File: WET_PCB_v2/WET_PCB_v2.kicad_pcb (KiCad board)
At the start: 2 copper layers, 100 x 80 mm, 164 parts, among them J1 Capacitor connector, J10 Conn_01x09_Pin, J11 Conn_01x09_Pin, J12 Fuse holder or smth to hold t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, J13 Fuse holder or smth to hold t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, J14 Fuse holder or smth to hold t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, J15 Fuse holder or smth to hold t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, J16 POGO1, J17 Capacitor connector, J18 Capacitor connector, J19 Capacitor connector, J2 Conn_01x09_Pin, J20 Capacitor connector, J21 POGO2, J22 LA55_GND, J23 LA55_M, J24 LA55_+, J25 Capacitor connector, J26 Vsense_ADC1_IN1, J27 Fuse holder or smth to hold t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, J28 Fuse holder or smth to hold t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, J29 Fuse holder or smth to hold t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, J3 Conn_01x09_Pin, J30 Fuse holder or smth to hold t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, J31 Fuse holder or smth to hold t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, J32 Fuse holder or smth to hold t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, J33 Fuse holder or smth to hold t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, J34 Fuse holder or smth to hold t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, J4 Power input, J5 Barrel jack, J6 Coil plug, J7 Pluggable Terminal Block, J8 Jumper, J9 Capacitor connector, Q1 IRF530NPBF, Q2 IRF530NPBF, Q3 IRF530NPBF, Q4 IRF530NPBF, Q5 Q_NMOS_GDS, Q6 Q_NMOS_GDS, U1 IR2110, U2 IR2110, U3 Opamp_Quad, U4 IR2110, U5 LA55-P, U6 L7805

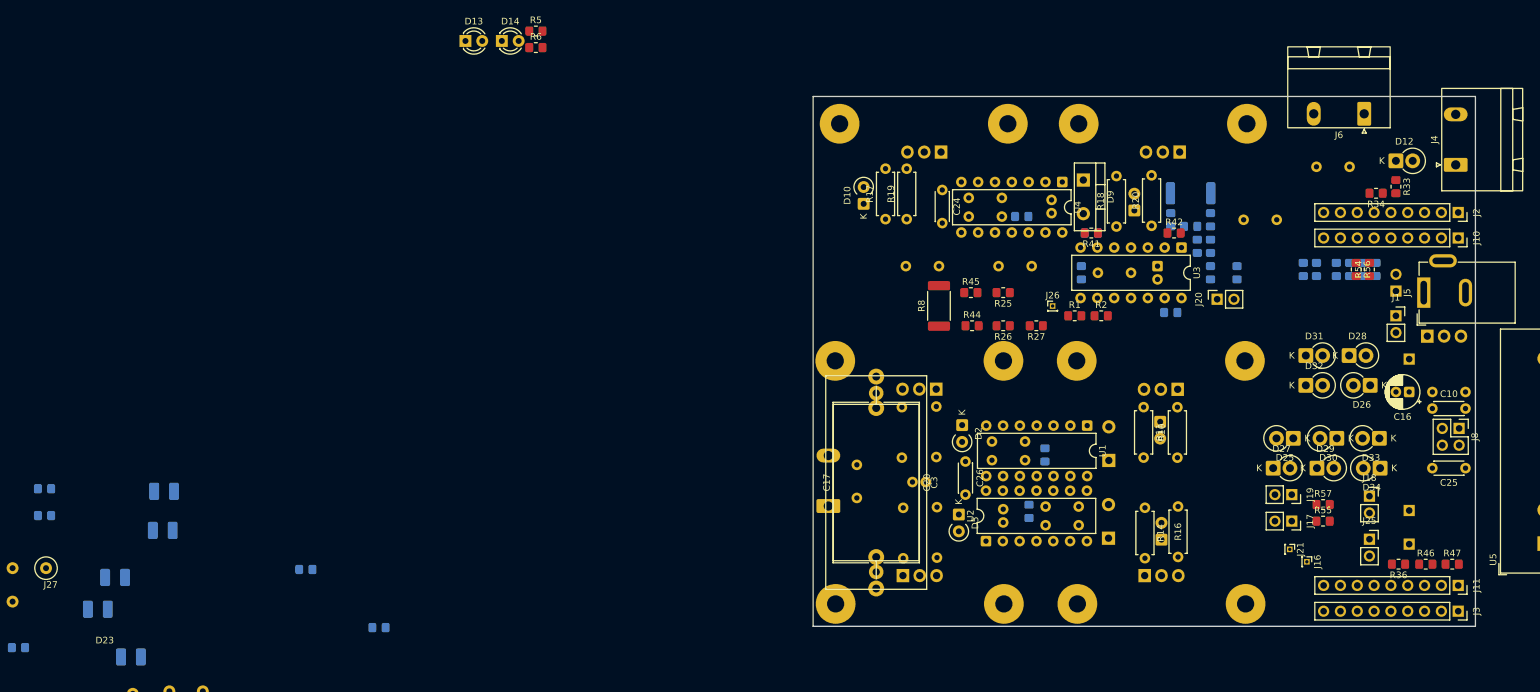
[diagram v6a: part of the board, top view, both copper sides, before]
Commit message: microcontroller to chip traces done
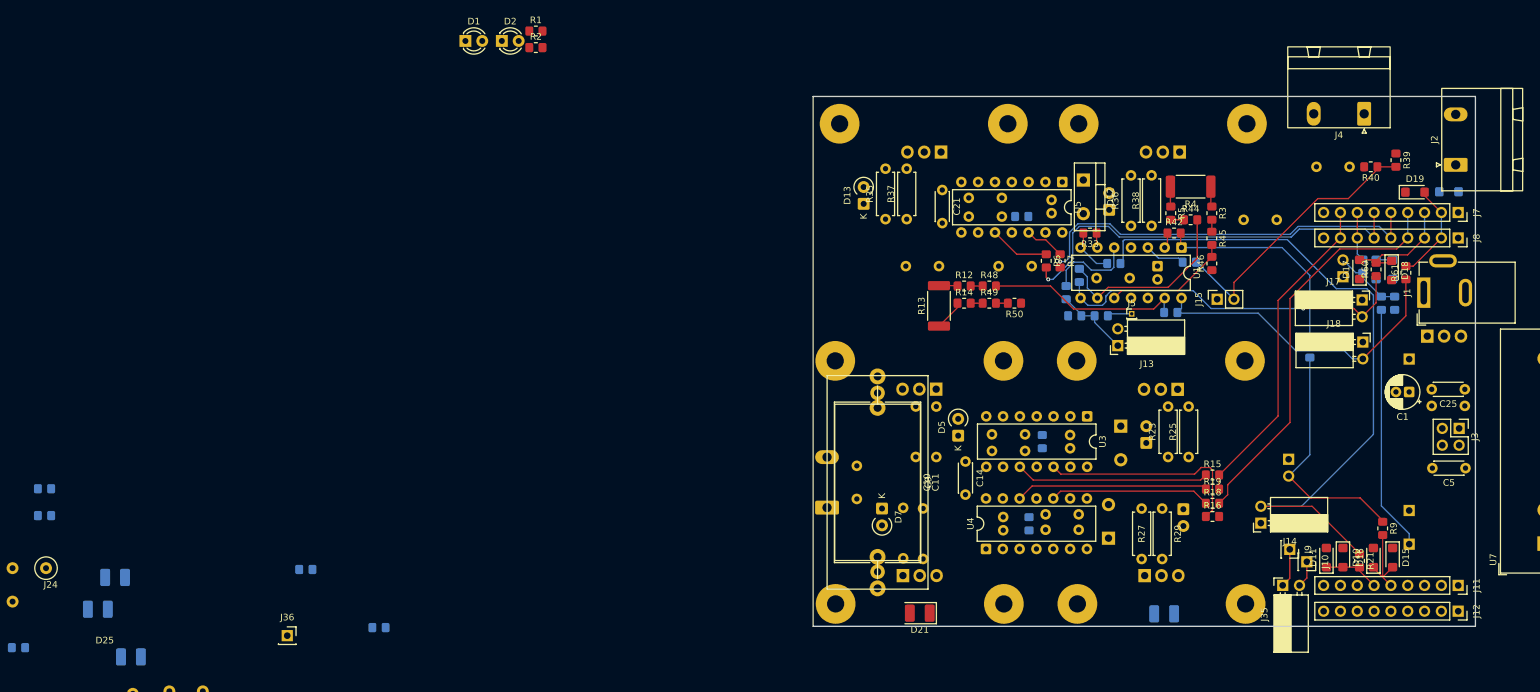
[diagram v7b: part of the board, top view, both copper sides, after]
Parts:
- removed the C17 at (167.5, 154.7)
- removed the C20 at (167.5, 127.4)
- removed the D12 at (246.0, 90.1)
- removed D33, D34: D_Zener, Diode_THT:D_DO-15_P2.54mm_Vertical_CathodeUp
- removed the R54 at (242.0, 106.5)
- removed the R55 at (235.0, 144.5)
- removed the R56 at (240.0, 106.5)
- removed the R57 at (235.0, 142.0)
- added C10: B32529C1104K000, Inductor_THT:L_Axial_L23.4mm_D12.7mm_P32.00mm_Horizontal_Vishay_IHA-203, F.Cu at (167.7, 122.7)
- added C9: B32529C1104K000, Capacitor_THT:C_Rect_L24.0mm_W12.8mm_P22.50mm_MKT, F.Cu at (167.7, 127.4)
- added D27: D_Zener, Diode_SMD:D_SMF, B.Cu at (243.0, 106.5)
- added D28: D_Zener, Diode_SMD:D_SMF, B.Cu at (245.5, 106.5)
- added J35: Programming, Connector_PinSocket_2.54mm:PinSocket_1x02_P2.54mm_Horizontal, F.Cu at (228.9, 154.2)
- added J36: LED_POWER, Connector_PinSocket_2.54mm:PinSocket_1x01_P2.54mm_Vertical, F.Cu at (78.6, 161.8)
- added R10: R0, Resistor_SMD:R_0805_2012Metric_Pad1.20x1.40mm_HandSolder, B.Cu at (241.0, 106.0)
- added R21: R0, Resistor_SMD:R_0805_2012Metric_Pad1.20x1.40mm_HandSolder, F.Cu at (240.5, 150.5)
- added R60: R0, Resistor_SMD:R_0805_2012Metric_Pad1.20x1.40mm_HandSolder, F.Cu at (243.0, 106.5)
- added R61: R0, Resistor_SMD:R_0805_2012Metric_Pad1.20x1.40mm_HandSolder, F.Cu at (247.5, 107.0)
- added R9: R0, Resistor_SMD:R_0805_2012Metric_Pad1.20x1.40mm_HandSolder, F.Cu at (244.0, 145.6)
- D10: renamed from D31; footprint Diode_THT:D_DO-15_P2.54mm_Vertical_CathodeUp -> Diode_SMD:D_SMF
- D11: renamed from D32; footprint Diode_THT:D_DO-15_P2.54mm_Vertical_CathodeUp -> Diode_SMD:D_SMF
- D15: renamed from D30; footprint Diode_THT:D_DO-15_P2.54mm_Vertical_CathodeUp -> Diode_SMD:D_SMF
- D16: renamed from D29; footprint Diode_THT:D_DO-15_P2.54mm_Vertical_CathodeUp -> Diode_SMD:D_SMF
- D17: renamed from D25; footprint Diode_THT:D_DO-15_P2.54mm_Vertical_CathodeUp -> Diode_SMD:D_SMF
- D18: renamed from D27; footprint Diode_THT:D_DO-15_P2.54mm_Vertical_CathodeUp -> Diode_SMD:D_SMF
- D19: renamed from D26; footprint Diode_THT:D_DO-15_P2.54mm_Vertical_CathodeUp -> Diode_SMD:D_SMF
- D20: renamed from D28; footprint Diode_THT:D_DO-15_P2.54mm_Vertical_CathodeUp -> Diode_SMD:D_SMF; moved to B.Cu
- D21: renamed from D19; moved to F.Cu
- J10: renamed from J16; footprint Connector_PinHeader_1.00mm:PinHeader_1x01_P1.00mm_Vertical -> Connector_PinSocket_2.54mm:PinSocket_1x01_P2.54mm_Vertical
- J13: renamed from J19; footprint Connector_PinSocket_2.54mm:PinSocket_1x02_P2.54mm_Vertical -> Connector_PinSocket_2.54mm:PinSocket_1x02_P2.54mm_Horizontal
- J14: renamed from J17; footprint Connector_PinSocket_2.54mm:PinSocket_1x02_P2.54mm_Vertical -> Connector_PinSocket_2.54mm:PinSocket_1x02_P2.54mm_Horizontal
- J16: renamed from J18; footprint Connector_PinSocket_2.54mm:PinSocket_1x02_P2.54mm_Vertical -> Connector_PinSocket_2.54mm:PinSocket_1x02_P2.54mm_Horizontal; moved to B.Cu
- J17: renamed from J1; footprint Connector_PinSocket_2.54mm:PinSocket_1x02_P2.54mm_Vertical -> Connector_PinSocket_2.54mm:PinSocket_1x02_P2.54mm_Horizontal
- J18: renamed from J9; footprint Connector_PinSocket_2.54mm:PinSocket_1x02_P2.54mm_Vertical -> Connector_PinSocket_2.54mm:PinSocket_1x02_P2.54mm_Horizontal; moved to F.Cu
- J34: renamed from J25; footprint Connector_PinSocket_2.54mm:PinSocket_1x02_P2.54mm_Vertical -> Connector_PinSocket_2.54mm:PinSocket_1x02_P2.54mm_Horizontal; moved to B.Cu
- J9: renamed from J21; footprint Connector_PinHeader_1.00mm:PinHeader_1x01_P1.00mm_Vertical -> Connector_PinSocket_2.54mm:PinSocket_1x01_P2.54mm_Vertical
- R15: renamed from R50; moved to F.Cu
- R16: renamed from R51; moved to F.Cu
- R18: renamed from R52; moved to F.Cu
- R19: renamed from R53; moved to F.Cu
- R3: renamed from R37; moved to F.Cu
- R30: renamed from R1; moved to B.Cu
- R31: renamed from R2; moved to B.Cu
- R4: renamed from R7; moved to F.Cu
- R43: renamed from R36; moved to B.Cu
- R44: renamed from R21; moved to F.Cu
- R45: renamed from R23; moved to F.Cu
- R46: renamed from R24; moved to F.Cu
- R5: renamed from R43; moved to F.Cu
- R58: renamed from R46; moved to B.Cu
- R59: renamed from R47; moved to B.Cu
- R6: renamed from R48; moved to F.Cu
- R7: renamed from R49; moved to F.Cu
- moved D23 151.7 mm to (211.0, 158.5)
- moved D21 115.6 mm to (174.1, 158.4)
- moved R6 43.8 mm to (193.2, 105.2)
- moved R7 43.7 mm to (195.3, 105.2), turned to -90 degrees
- moved R16 43.7 mm to (218.3, 143.8), turned to 0 degrees
- moved R18 43.1 mm to (218.3, 141.8), turned to 0 degrees
- moved R59 40.3 mm to (245.8, 111.6), turned to 90 degrees
- moved R58 40.0 mm to (243.8, 111.6), turned to 90 degrees
- moved J34 39.8 mm to (238.0, 107.6)
- moved R19 36.7 mm to (218.3, 139.7), turned to 0 degrees
- moved R43 34.9 mm to (233.0, 118.8), turned to -90 degrees
- moved D18 34.8 mm to (245.3, 106.7), turned to -90 degrees
- moved J13 34.6 mm to (204.0, 118.0), turned to 180 degrees
- moved R15 33.9 mm to (218.3, 137.5), turned to 0 degrees
- moved D10 31.0 mm to (238.0, 150.0), turned to -90 degrees
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- renumbered C16 to C1, C3 to C11, C7 to C12, C6 to C13, C26 to C14, C5 to C15, C11 to C16, C22 to C17, C12 to C18, C23 to C19, C18 to C2, C13 to C20, C24 to C21, C14 to C22, C15 to C23, C9 to C24, C10 to C25, C19 to C3, C1 to C4, C25 to C5, C2 to C6, C4 to C7, D13 to D1, D9 to D12, D10 to D13, D11 to D14, D14 to D2, D20 to D22, D21 to D23, D22 to D24, D23 to D25, D24 to D26, D1 to D4, D2 to D5, D3 to D6, D5 to D7, D6 to D8, D4 to D9, HS3 to HS1, HS5 to HS2, HS4 to HS3, HS6 to HS4, HS2 to HS5, HS1 to HS6, J5 to J1, J3 to J12, J20 to J15, J12 to J19, J4 to J2, J13 to J20, J14 to J21, J15 to J22, J28 to J23, J27 to J24, J29 to J25, J30 to J26, J31 to J27, J32 to J28, J33 to J29, J8 to J3, J34 to J30, J22 to J31, J24 to J32, J23 to J33, J6 to J4, J26 to J5, J7 to J6, J2 to J7, J10 to J8, R5 to R1, R45 to R12, R8 to R13, R44 to R14, R39 to R17, R6 to R2, R40 to R20, R9 to R22, R10 to R23, R12 to R24, R11 to R25, R15 to R26, R16 to R27, R13 to R28, R14 to R29, R3 to R32, R41 to R33, R4 to R34, R17 to R35, R18 to R36, R19 to R37, R20 to R38, R33 to R39, R34 to R40, R35 to R41, R22 to R47, R25 to R48, R26 to R49, R27 to R50, R28 to R51, R29 to R52, R30 to R53, R31 to R54, R32 to R55, R58 to R56, R59 to R57, R38 to R8, U3 to U1, U1 to U3, U2 to U4, U4 to U5, U5 to U7
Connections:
- net /curr_sense_coil/transducer_out_scaled renamed Net-(J34-Pin_2)
- C20 pad 2: /DCDC/Gatedriver/VDD_Driver_DCDC -> +5V
- C21 pad 2: /DCDC/Gatedriver/VDD_Driver_DCDC -> +5V
- D10 pad 2: /voltsense_inverter/Vsense_ADC -> /ADC1_IN1
- D11 pad 1: /voltsense_inverter/Vsense_ADC -> /ADC1_IN1
- D12 pad 2: /DCDC/Gatedriver/VCC_Driver -> +12V
- D15 pad 1: /voltsense_DCDC/VDD_OPAMP -> +5V
- D15 pad 2: /voltsense_DCDC/Vsense_ADC -> /ADC1_IN0
- D16 pad 1: /voltsense_DCDC/Vsense_ADC -> /ADC1_IN0
- D17 pad 2: /currsense_DCDC/currsense_ADC -> /ADC1_IN5
- D18 pad 1: /currsense_DCDC/currsense_ADC -> /ADC1_IN5
- J13 pad 1: GND -> Net-(J13-Pin_1)
- J13 pad 2: Net-(J19-Pin_2) -> GND
- J14 pad 2: /voltsense_inverter/Vsense_ADC -> Net-(J14-Pin_2)
- J16 pad 2: /voltsense_DCDC/Vsense_ADC -> Net-(J16-Pin_2)
- J17 pad 2: /currsense_DCDC/currsense_ADC -> Net-(J17-Pin_2)
- J18 pad 2: /ADC1_IN4 -> Net-(J18-Pin_2)
- J2 pad 1: Net-(D12-A) -> VPP
- R30 pad 2: Net-(J19-Pin_2) -> Net-(J13-Pin_1)
- R31 pad 1: Net-(J19-Pin_2) -> Net-(J13-Pin_1)
- R32 pad 1: Net-(J19-Pin_2) -> Net-(J13-Pin_1)
- R34 pad 2: /voltsense_inverter/Vsense_ADC -> Net-(J14-Pin_2)
- R39 pad 1: /voltsense_DCDC/Vsense_in -> VPP
- R43 pad 2: /voltsense_DCDC/Vsense_ADC -> Net-(J16-Pin_2)
- R47 pad 2: /currsense_DCDC/currsense_ADC -> Net-(J17-Pin_2)
- R51 pad 2: /ADC1_IN4 -> Net-(J18-Pin_2)
- R52 pad 2: /TIM1_CH4 -> /decoration/UVLED1
- R53 pad 2: /TIM1_CH4 -> /decoration/UVLED1
- R54 pad 2: /TIM1_CH4 -> /decoration/UVLED1
- R55 pad 2: /TIM1_CH4 -> /decoration/UVLED1
- R56 pad 2: /TIM1_CH4 -> /decoration/UVLED1
- R57 pad 2: /TIM1_CH4 -> /decoration/UVLED1
- U1 pad 14: /ADC1_IN4 -> Net-(J18-Pin_2)
- U1 pad 8: /currsense_DCDC/currsense_ADC -> Net-(J17-Pin_2)
- U5 pad 10: /DCDC/Gatedriver/DCDC_Driver_Hin -> /DCDC/DCDC_Driver_Hin
- U5 pad 11: /DCDC/Gatedriver/DCDC_Driver_SD -> /DCDC/DCDC_Driver_SD
- U5 pad 12: /DCDC/Gatedriver/DCDC_Driver_Lin -> /DCDC/DCDC_Driver_Lin
- U5 pad 3: /DCDC/Gatedriver/VCC_Driver -> +12V
- U5 pad 9: /DCDC/Gatedriver/VDD_Driver_DCDC -> +5V
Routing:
- net Net-(J14-Pin_2): track 0.00 -> 105.4 mm
- net /TIM1_CH4: track 0.00 -> 62.4 mm, vias 0 -> 1
- net /TIM14_CH1: track 0.00 -> 61.2 mm, vias 0 -> 1
- net /TIM3_CH2: track 0.00 -> 60.8 mm
- net Net-(J17-Pin_2): track 0.00 -> 55.8 mm, vias 0 -> 1
- net /TIM3_CH1: track 0.00 -> 49.4 mm
- net Net-(J18-Pin_2): track 0.00 -> 48.0 mm
- net Net-(J15-Pin_2): track 0.00 -> 42.3 mm
- net Net-(J33-Pin_1): track 0.00 -> 37.1 mm
- net Net-(J16-Pin_2): track 0.00 -> 36.5 mm
- net Net-(R42-Pad2): track 0.00 -> 33.8 mm
- net /inverter/Inv_Driver_Left_Lin: track 0.00 -> 32.4 mm
- net Net-(U1D-in4-): track 0.00 -> 29.8 mm
- net /inverter/Inv_Driver_Left_Hin: track 0.00 -> 29.2 mm
- net /inverter/Inv_Driver_Right_Lin: track 0.00 -> 29.1 mm
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
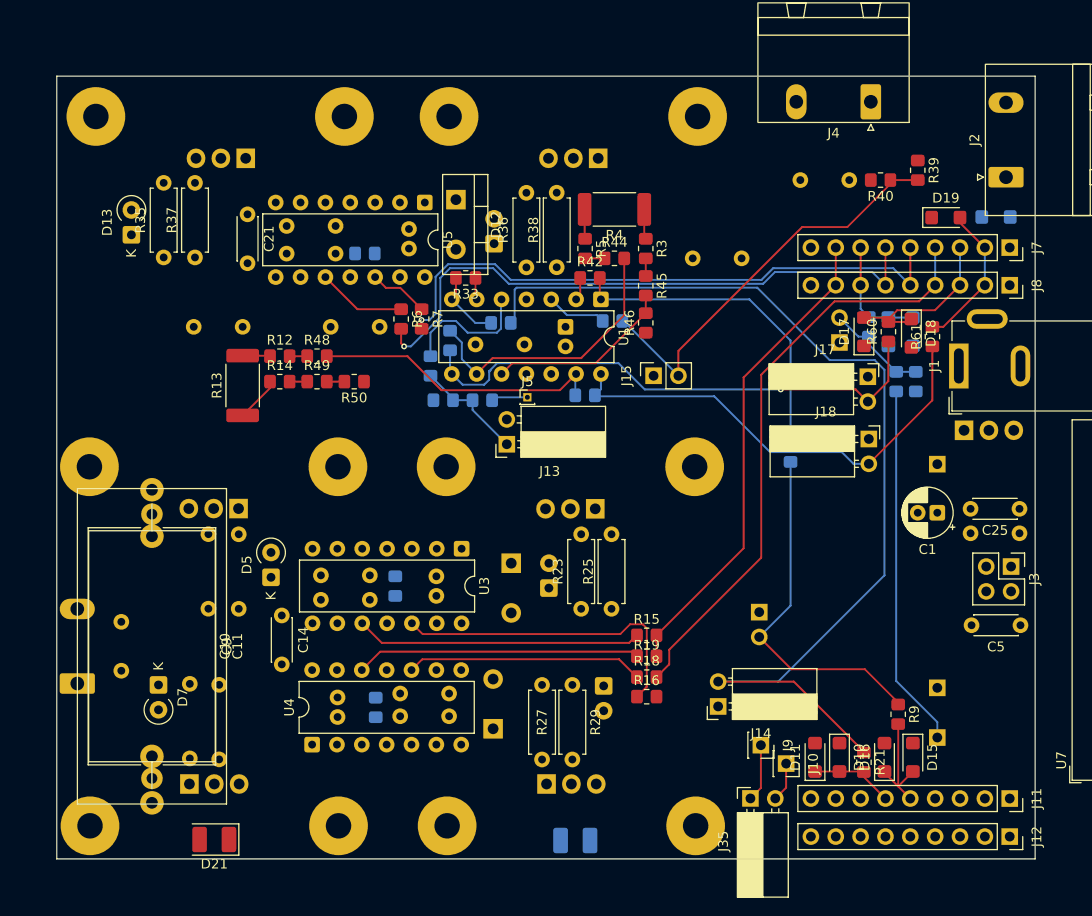
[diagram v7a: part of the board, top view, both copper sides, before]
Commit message: most routing done. to do: 12v routing, test points, deco, checking clearance
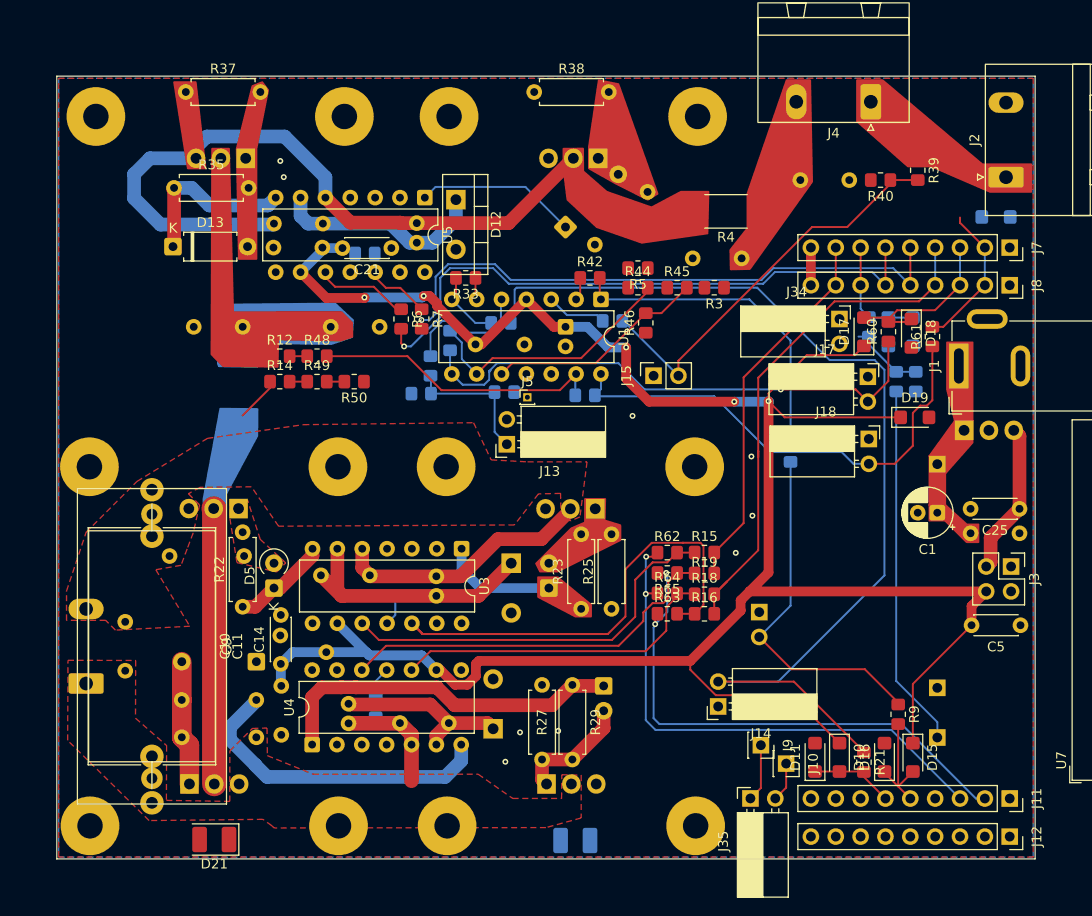
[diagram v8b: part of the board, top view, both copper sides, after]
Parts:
- added R62: R0, Resistor_SMD:R_0805_2012Metric_Pad1.20x1.40mm_HandSolder, F.Cu at (220.4, 129.1)
- added R63: R0, Resistor_SMD:R_0805_2012Metric_Pad1.20x1.40mm_HandSolder, F.Cu at (220.4, 135.3)
- added R64: R0, Resistor_SMD:R_0805_2012Metric_Pad1.20x1.40mm_HandSolder, F.Cu at (220.4, 133.2)
- added R65: R0, Resistor_SMD:R_0805_2012Metric_Pad1.20x1.40mm_HandSolder, F.Cu at (220.4, 131.2)
- D13, D14: footprint Diode_THT:D_A-405_P2.54mm_Vertical_CathodeUp -> Diode_THT:D_A-405_P7.62mm_Horizontal
- D7: footprint Diode_THT:D_A-405_P2.54mm_Vertical_CathodeUp -> Diode_THT:D_A-405_P7.62mm_Horizontal; moved to B.Cu
- J34, R22: moved to F.Cu
- R13, R36: moved to B.Cu
- moved D19 20.7 mm to (245.7, 115.2)
- moved R38 18.1 mm to (206.8, 82.0), turned to 0 degrees
- moved R37 16.9 mm to (171.2, 82.0), turned to 0 degrees
- moved C21 15.1 mm to (192.2, 98.0), turned to 180 degrees
- moved C15 12.9 mm to (180.9, 147.7), turned to 90 degrees
- moved R4 11.4 mm to (226.4, 94.2)
- moved R15 10.3 mm to (224.2, 129.1)
- moved R16 10.3 mm to (224.2, 135.3)
- moved R18 10.3 mm to (224.2, 133.3)
- moved R19 10.3 mm to (224.2, 131.2)
- moved D7 10.3 mm to (178.4, 140.2), turned to 180 degrees
- moved C4 9.85 mm to (180.9, 137.5), turned to -20 degrees
- moved R3 8.06 mm to (225.2, 102.0), turned to 180 degrees
- moved D14 7.50 mm to (210.0, 95.8), turned to 45 degrees
- moved R36 7.37 mm to (213.0, 97.6), turned to 45 degrees
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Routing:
- net +5V: track 0.00 -> 236.2 mm, vias 0 -> 5
- net /DCDC/currsense_FET_side: track 3.02 -> 72.7 mm
- net /TIM17_CH1: track 0.00 -> 55.1 mm, vias 0 -> 2
- net /TIM17_CH1N: track 0.00 -> 54.6 mm, vias 0 -> 2
- net Net-(D8-K): track 0.00 -> 36.7 mm
- net /inverter/Inv_Driver_Left_Lin: track 32.4 -> 66.3 mm
- net Net-(D7-K): track 0.00 -> 32.6 mm
- net /inverter/Vin_Inverter: track 4.61 -> 32.9 mm
- net Net-(C7--): track 0.00 -> 26.8 mm
- net /inverter/Vout_Inverter_+: track 0.00 -> 26.5 mm
- net Net-(C23--): track 0.00 -> 21.9 mm
- net Net-(C12--): track 0.00 -> 18.6 mm
- net Net-(D13-K): track 0.00 -> 17.6 mm
- net Net-(D14-K): track 0.00 -> 16.5 mm
- net /12V_to5V/Vout_5V: track 0.00 -> 15.6 mm
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- added copper zone on F.Cu, net /inverter/Vout_Inverter_+
- added copper zone on F.Cu, net /inverter/Vout_Inverter_-
- added copper zone on B.Cu, net GND
- added copper zone on F.Cu, net GND
- added copper zone on F.Cu, net Net-(D5-A)
